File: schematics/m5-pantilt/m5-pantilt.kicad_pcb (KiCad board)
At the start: 2 copper layers, 50 x 50 mm, 28 parts, among them J1 Conn_02x15_Odd_Even, J2 Conn_02x03_Odd_Even, J3 Conn_02x03_Odd_Even, J4 Conn_01x04, J5 BAT, J6 Conn_01x04, J7 5V_POWER, SW1 SW_SPDT, U1 NL27WZ125

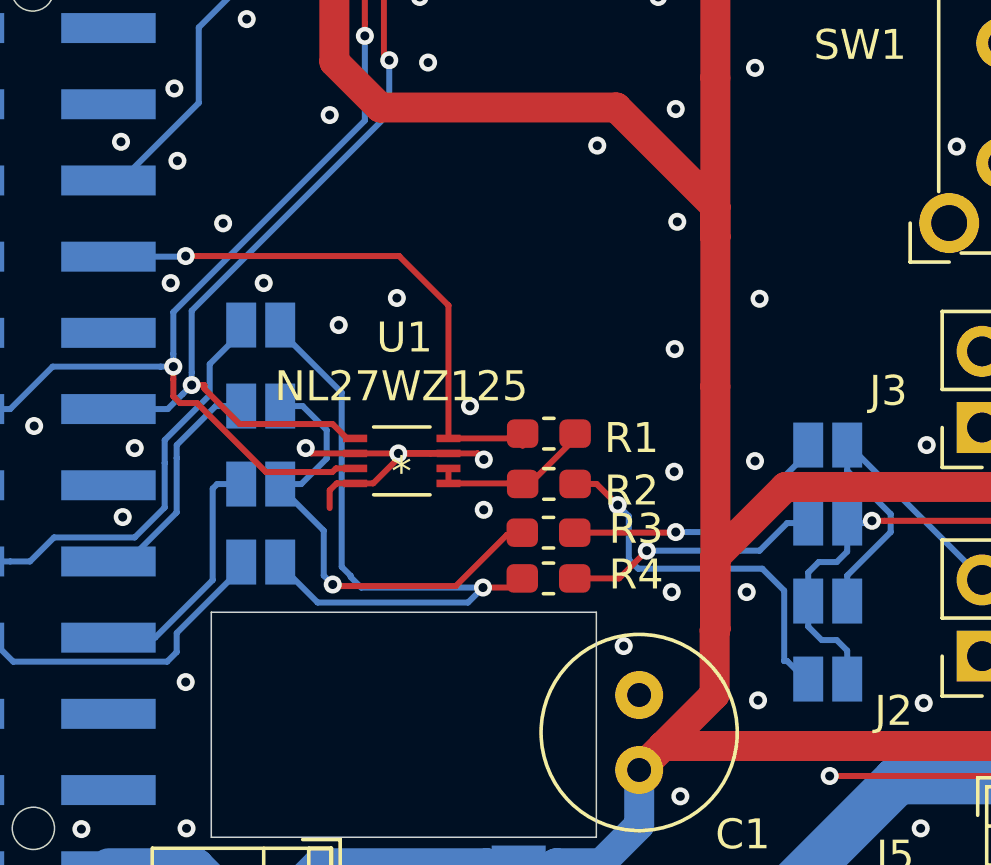
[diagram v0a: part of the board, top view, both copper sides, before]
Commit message: Update to v0.2.0
Support another Three-State Bus Buffers, TC7WH241FK
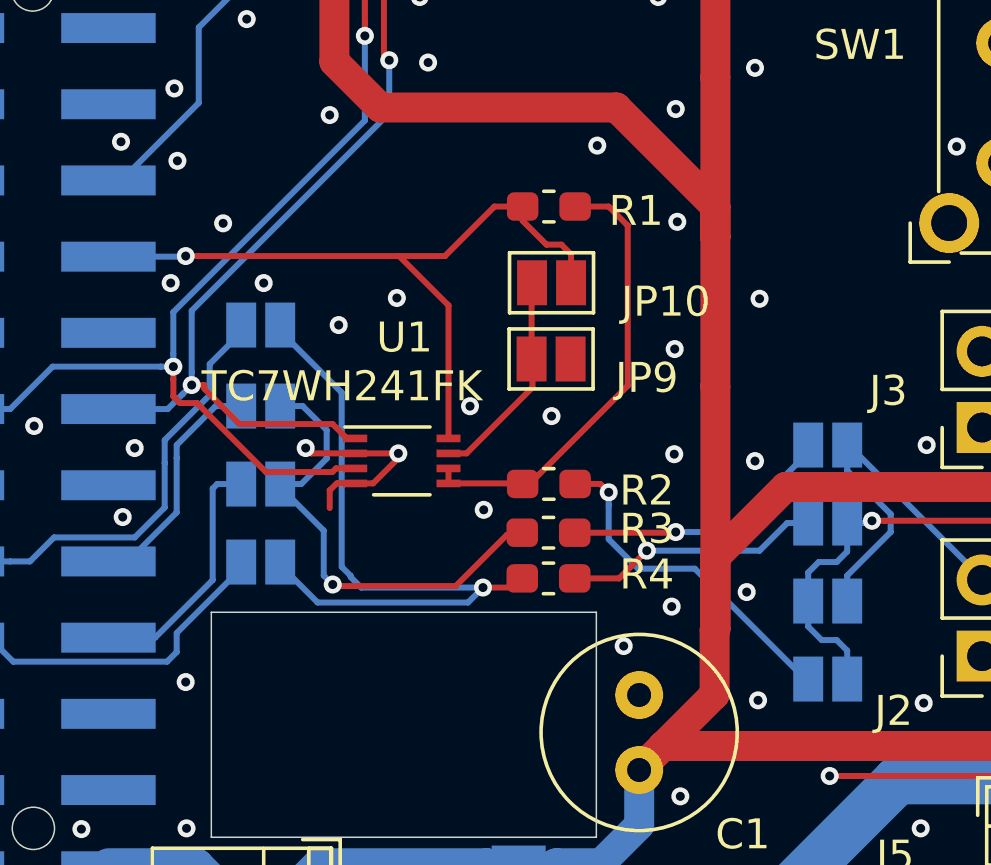
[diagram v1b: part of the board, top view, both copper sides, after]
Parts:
- added JP10: Jumper_2_Open, Jumper:SolderJumper-2_P1.3mm_Open_Pad1.0x1.5mm, F.Cu at (123.5, 70.8)
- added JP9: Jumper_2_Open, Jumper:SolderJumper-2_P1.3mm_Open_Pad1.0x1.5mm, F.Cu at (123.5, 73.3)
- U1: value NL27WZ125 -> TC7WH241FK
- moved R1 7.57 mm to (123.4, 68.2)
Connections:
- U1 pad 7: GND -> Net-(JP10-Pad2)
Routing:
- net Net-(R1-Pad2): track 5.20 -> 15.4 mm
- net Net-(JP10-Pad2): track 0.00 -> 7.92 mm
- net +3V3: track 19.0 -> 25.1 mm
- net GND: track 11.2 -> 6.71 mm
- net Net-(JP4-Pad2): track 12.7 -> 11.4 mm
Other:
- board text added: "fork of v0.1.1 designed by @meganetaaan"
- board text added: "m5-pantilt board v0.2.0 @Tiryoh"
- board text removed: "m5-pantilt board v0.1.1 @meganetaaan"

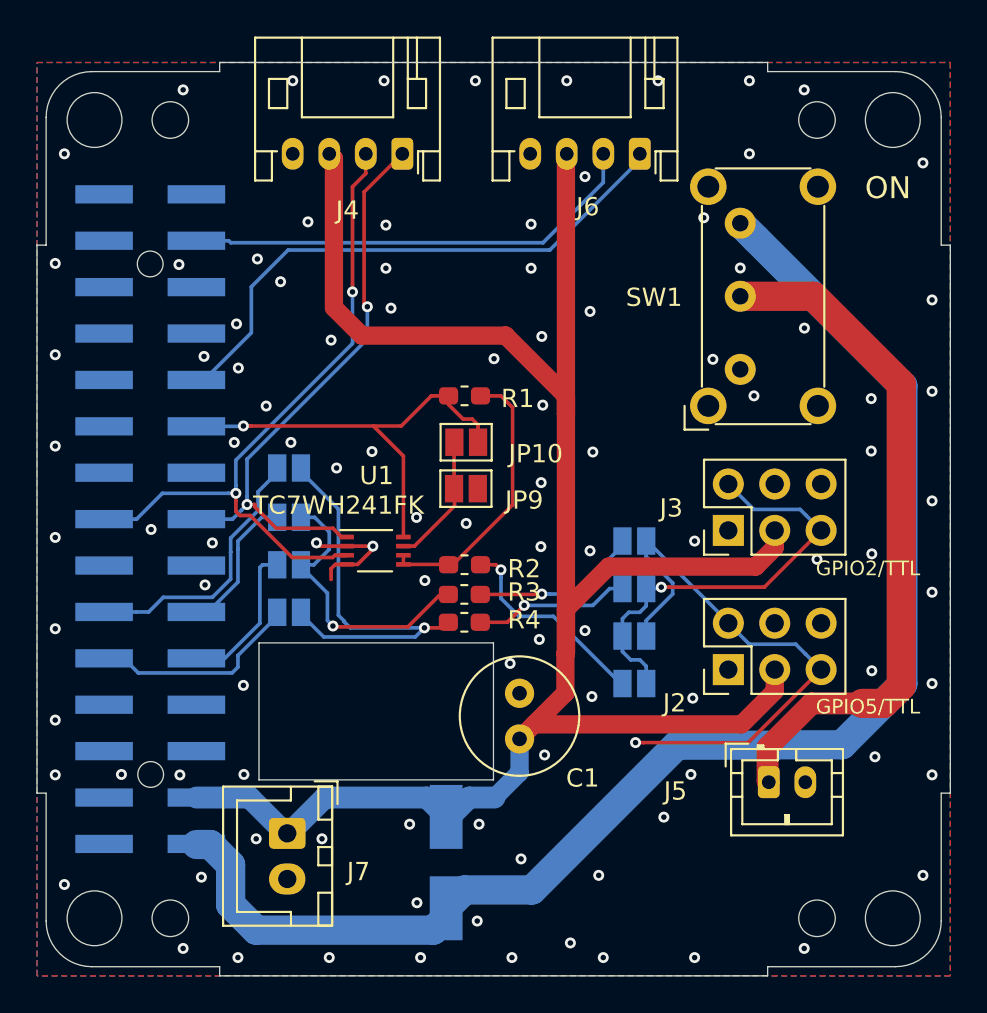
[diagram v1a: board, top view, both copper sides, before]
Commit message: Update to v0.2.1
Add description to schematic and PCB
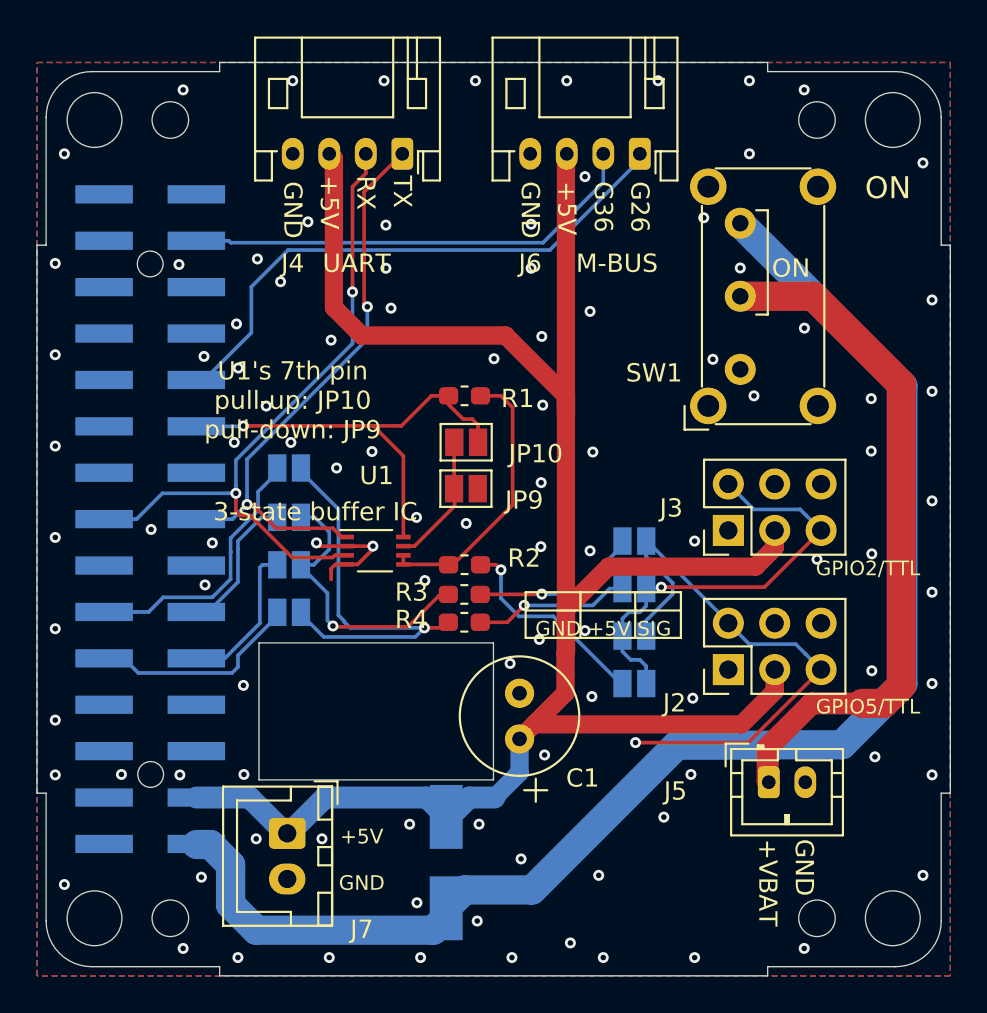
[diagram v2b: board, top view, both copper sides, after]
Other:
- board text added: "+5V"
- board text added: "+VBAT"
- board text added: "3-state buffer IC"
- board text added: "G26"
- board text added: "G36"
- board text added: "GND"
- board text added: "GND +5V SIG"
- board text added: "M-BUS"
- board text added: "RX"
- board text added: "TX"
- board text added: "U1's 7th pin pull-up: JP10 pull-down: JP9"
- board text added: "UART"
- board text added: "m5-pantilt board v0.2.1 @Tiryoh"
- board text removed: "m5-pantilt board v0.2.0 @Tiryoh"
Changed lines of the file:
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@@
   (general
     (thickness 1.6)
-    (drawings 49)
+    (drawings 79)
     (tracks 366)
     (zones 0)
@@
       (effects (font (size 1 1) (thickness 0.15)))
     )
-    (fp_text value TC7WH241FK (at -1.994 -2.4838 180) (layer F.SilkS)
+    (fp_text value TC7WH241FK (at -1.994 -2.4838 180) (layer F.SilkS) hide
       (effects (font (size 1 1) (thickness 0.15)))
     )
@@
     (descr "JST PH series connector, S4B-PH-K (http://www.jst-mfg.com/product/pdf/eng/ePH.pdf), generated with kicad-footprint-generator")
     (tags "connector JST PH top entry")
-    (fp_text reference J6 (at 2.8476 -2.9056) (layer F.SilkS)
+    (fp_text reference J6 (at 6 -6) (layer F.SilkS)
       (effects (font (size 1 1) (thickness 0.15)))
     )
@@
     (tags "resistor handsolder")
     (attr smd)
-    (fp_text reference R2 (at -3.264 -0.2246) (layer F.SilkS)
+    (fp_text reference R2 (at -3.264 0.3556) (layer F.SilkS)
       (effects (font (size 1 1) (thickness 0.15)))
     )
@@
     (descr "E-Switch slide switch, EG series, SPDT, right angle, http://spec_sheets.e-switch.com/specs/P040042.pdf")
     (tags "switch SPDT")
-    (fp_text reference SW1 (at 3.9348 -4.718 180) (layer F.SilkS)
+    (fp_text reference SW1 (at -0.2 -4.718 180) (layer F.SilkS)
       (effects (font (size 1 1) (thickness 0.15)))
     )
@@
     (descr "JST PH series connector, S4B-PH-K (http://www.jst-mfg.com/product/pdf/eng/ePH.pdf), generated with kicad-footprint-generator")
     (tags "connector JST PH top entry")
-    (fp_text reference J4 (at 3 -3.09) (layer F.SilkS)
+    (fp_text reference J4 (at 6 -6) (layer F.SilkS)
       (effects (font (size 1 1) (thickness 0.15)))
     )
@@
     (tags "resistor handsolder")
     (attr smd)
-    (fp_text reference R3 (at -3.2766 0.127) (layer F.SilkS)
+    (fp_text reference R3 (at 2.8934 0.1212) (layer F.SilkS)
       (effects (font (size 1 1) (thickness 0.15)))
     )
@@
     (tags "resistor handsolder")
     (attr smd)
-    (fp_text reference R4 (at -3.2766 0.127) (layer F.SilkS)
+    (fp_text reference R4 (at 2.8934 0.1452) (layer F.SilkS)
       (effects (font (size 1 1) (thickness 0.15)))
     )
@@
     (descr "JST XH series connector, B2B-XH-A (http://www.jst-mfg.com/product/pdf/eng/eXH.pdf), generated with kicad-footprint-generator")
     (tags "connector JST XH vertical")
-    (fp_text reference J7 (at 2.1 -3.9 180) (layer F.SilkS)
+    (fp_text reference J7 (at 5.26 -4.08 180) (layer F.SilkS)
       (effects (font (size 1 1) (thickness 0.15)))
     )
@@
     )
   )
+  (gr_line (start 129.75 79) (end 129.75 81.5) (layer F.SilkS) (width 0.12))
+  (gr_line (start 132.75 79) (end 132.75 81.5) (layer F.SilkS) (width 0.12))
+  (gr_line (start 126.75 80) (end 135.25 80) (layer F.SilkS) (width 0.12))
+  (gr_line (start 126.75 79) (end 126.75 81.5) (layer F.SilkS) (width 0.12))
+  (gr_line (start 135.25 79) (end 126.75 79) (layer F.SilkS) (width 0.12))
+  (gr_line (start 135.25 81.5) (end 135.25 79) (layer F.SilkS) (width 0.12))
+  (gr_line (start 126.75 81.5) (end 135.25 81.5) (layer F.SilkS) (width 0.12))
+  (gr_text "GND +5V SIG" (at 131 81) (layer F.SilkS)
+    (effects (font (size 0.8 0.8) (thickness 0.15)))
+  )
+  (gr_text GND (at 127 56.5 270) (layer F.SilkS)
+    (effects (font (size 1 1) (thickness 0.15)) (justify left))
+  )
+  (gr_text +5V (at 129 56.5 270) (layer F.SilkS)
+    (effects (font (size 1 1) (thickness 0.15)) (justify left))
+  )
+  (gr_text G36 (at 131 56.5 270) (layer F.SilkS)
+    (effects (font (size 1 1) (thickness 0.15)) (justify left))
+  )
+  (gr_text G26 (at 133 56.5 270) (layer F.SilkS)
+    (effects (font (size 1 1) (thickness 0.15)) (justify left))
+  )
+  (gr_text GND (at 114 56.5 270) (layer F.SilkS)
+    (effects (font (size 1 1) (thickness 0.15)) (justify left))
+  )
+  (gr_text +5V (at 116 56.185 270) (layer F.SilkS)
+    (effects (font (size 1 1) (thickness 0.15)) (justify left))
+  )
+  (gr_text RX (at 118 56.185 270) (layer F.SilkS)
+    (effects (font (size 1 1) (thickness 0.15)) (justify left))
+  )
+  (gr_text TX (at 120 56.185 270) (layer F.SilkS)
+    (effects (font (size 1 1) (thickness 0.15)) (justify left))
+  )
+  (gr_text "3-state buffer IC" (at 115.24 74.6) (layer F.SilkS)
+    (effects (font (size 1 1) (thickness 0.15)))
+  )
+  (gr_text ON (at 141.275 61.265) (layer F.SilkS)
+    (effects (font (size 1 1) (thickness 0.15)))
+  )
+  (gr_line (start 140.005 63.805) (end 139.37 63.805) (layer F.SilkS) (width 0.12))
+  (gr_line (start 140.005 58.09) (end 140.005 63.805) (layer F.SilkS) (width 0.12))
+  (gr_line (start 139.37 58.09) (end 140.005 58.09) (layer F.SilkS) (width 0.12))
+  (gr_text GND (at 142 92.5 270) (layer F.SilkS)
+    (effects (font (size 1 1) (thickness 0.15)) (justify left))
+  )
+  (gr_text +VBAT (at 140 92.5 270) (layer F.SilkS)
+    (effects (font (size 1 1) (thickness 0.15)) (justify left))
+  )
+  (gr_text GND (at 117.78 94.92) (layer F.SilkS)
+    (effects (font (size 0.8 0.8) (thickness 0.15)))
+  )
+  (gr_text +5V (at 117.78 92.38) (layer F.SilkS)
+    (effects (font (size 0.8 0.8) (thickness 0.15)))
+  )
+  (gr_text UART (at 117.5 61) (layer F.SilkS)
+    (effects (font (size 1 1) (thickness 0.15)))
+  )
+  (gr_text M-BUS (at 131.75 61) (layer F.SilkS)
+    (effects (font (size 1 1) (thickness 0.15)))
+  )
+  (gr_text "U1's 7th pin\npull-up: JP10\npull-down: JP9" (at 114 68.5) (layer F.SilkS)
+    (effects (font (size 1 1) (thickness 0.15)))
+  )
+  (gr_line (start 127.305 89.205) (end 127.305 90.475) (layer F.SilkS) (width 0.12))
+  (gr_line (start 126.67 89.84) (end 127.94 89.84) (layer F.SilkS) (width 0.12))
   (dimension 50 (width 0.15) (layer Eco1.User)
     (gr_text "50.000 mm" (at 125 105.745) (layer Eco1.User)
@@
     (effects (font (size 1.2 1.2) (thickness 0.3)))
   )
-  (gr_text "m5-pantilt board v0.2.0\n@Tiryoh" (at 135.56 94.285) (layer B.SilkS)
+  (gr_text "m5-pantilt board v0.2.1\n@Tiryoh" (at 135.56 94.285) (layer B.SilkS)
     (effects (font (size 1.2 1.2) (thickness 0.3)) (justify mirror))
   )
@@
   (segment (start 133.35 76.2) (end 133.4 76.2) (width 0.2) (layer B.Cu) (net 24))
   (segment (start 133.4 76.2) (end 137.846 80.646) (width 0.2) (layer B.Cu) (net 24))
+  (segment (start 147.316001 67.610801) (end 147.316001 84.124001) (width 1.6) (layer F.Cu) (net 29))
+  (segment (start 142.5052 62.8) (end 147.316001 67.610801) (width 1.6) (layer F.Cu) (net 29))
+  (segment (start 138.5 62.8) (end 142.5052 62.8) (width 1.6) (layer F.Cu) (net 29))
+  (segment (start 147.316001 84.124001) (end 146.354001 85.086001) (width 1.6) (layer F.Cu) (net 29))
+  (segment (start 146.354001 85.086001) (end 145.171647 85.086001) (width 1.6) (layer F.Cu) (net 29))
+  (segment (start 145.171647 85.086001) (end 142.413999 85.086001) (width 1.2) (layer F.Cu) (net 29))
+  (segment (start 139.997199 87.502801) (end 139.997199 89.337199) (width 1.2) (layer F.Cu) (net 29))
+  (segment (start 142.413999 85.086001) (end 139.997199 87.502801) (width 1.2) (layer F.Cu) (net 29))
   (segment (start 139.997199 89.337199) (end 140.06 89.4) (width 1.2) (layer F.Cu) (net 29))
-  (segment (start 139.997199 87.502801) (end 139.997199 89.337199) (width 1.2) (layer F.Cu) (net 29))
-  (segment (start 145.171647 85.086001) (end 142.413999 85.086001) (width 1.2) (layer F.Cu) (net 29))
-  (segment (start 142.413999 85.086001) (end 139.997199 87.502801) (width 1.2) (layer F.Cu) (net 29))
-  (segment (start 146.354001 85.086001) (end 145.171647 85.086001) (width 1.6) (layer F.Cu) (net 29))
-  (segment (start 147.316001 84.124001) (end 146.354001 85.086001) (width 1.6) (layer F.Cu) (net 29))
-  (segment (start 147.316001 67.610801) (end 147.316001 84.124001) (width 1.6) (layer F.Cu) (net 29))
-  (segment (start 138.5 62.8) (end 142.5052 62.8) (width 1.6) (layer F.Cu) (net 29))
-  (segment (start 142.5052 62.8) (end 147.316001 67.610801) (width 1.6) (layer F.Cu) (net 29))
   (segment (start 120.05975 76.9782) (end 120.05975 77.478201) (width 0.2) (layer F.Cu) (net 30))
   (segment (start 124.281 68.25) (end 125.4 68.25) (width 0.2) (layer F.Cu) (net 30))
